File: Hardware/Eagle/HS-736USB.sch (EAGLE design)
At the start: 14 parts, among them Q1 12MHz

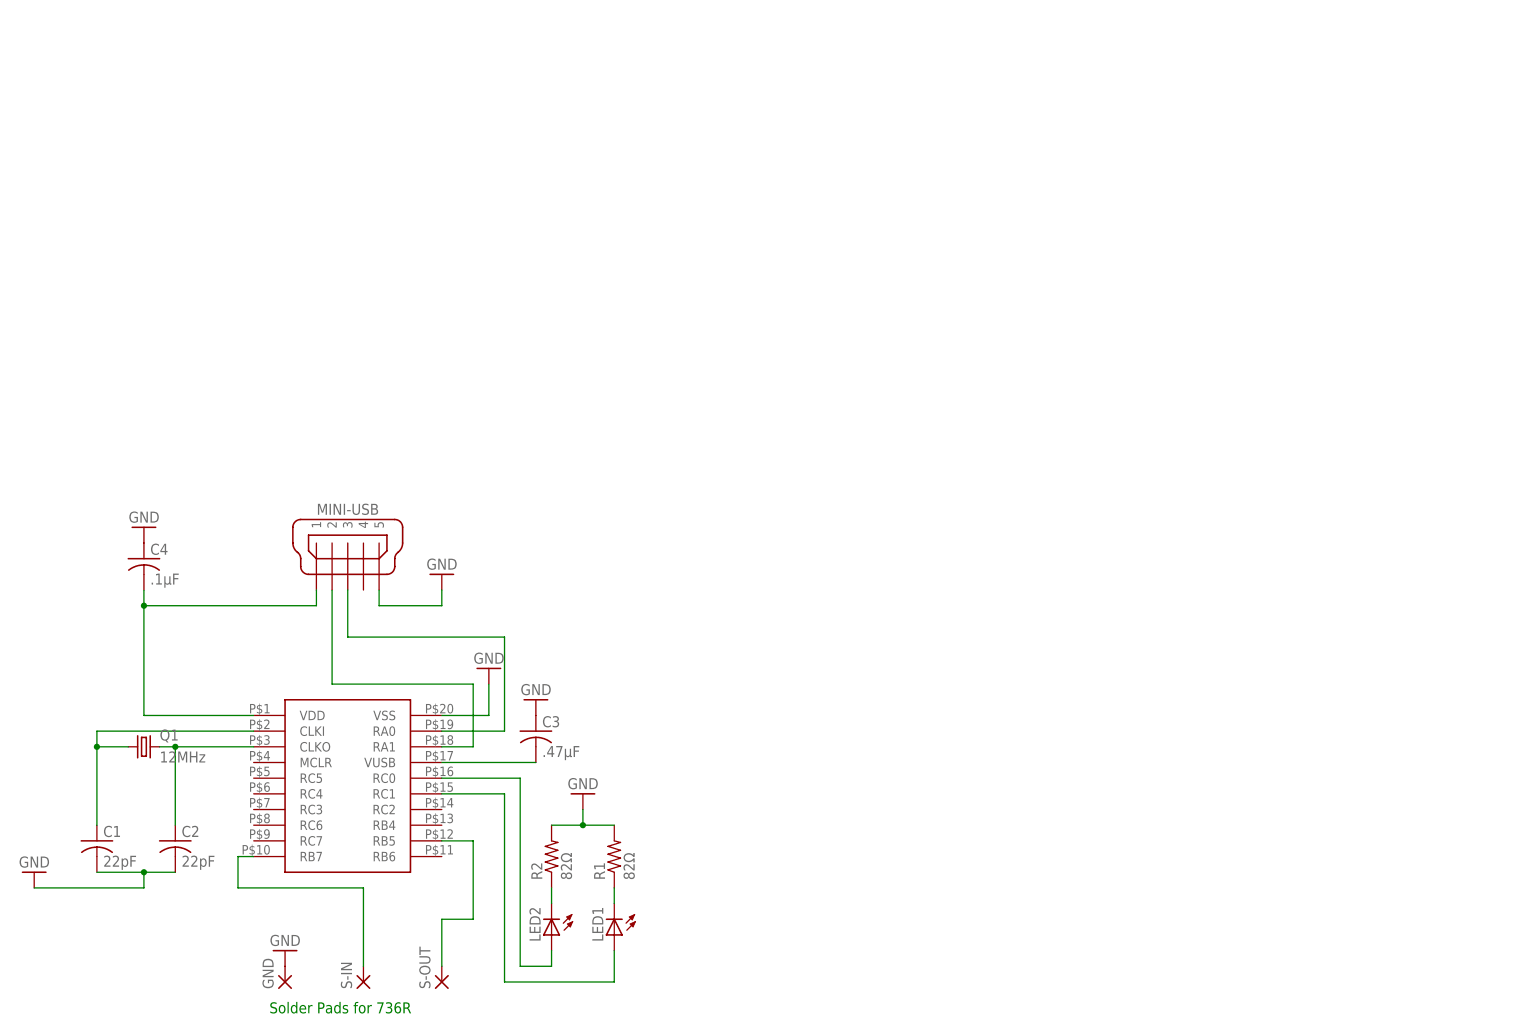
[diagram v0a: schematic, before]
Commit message: Updated schematic and board for a small board run August 2016.  Added missing Artwork for the various enclosure designs and board renderings.
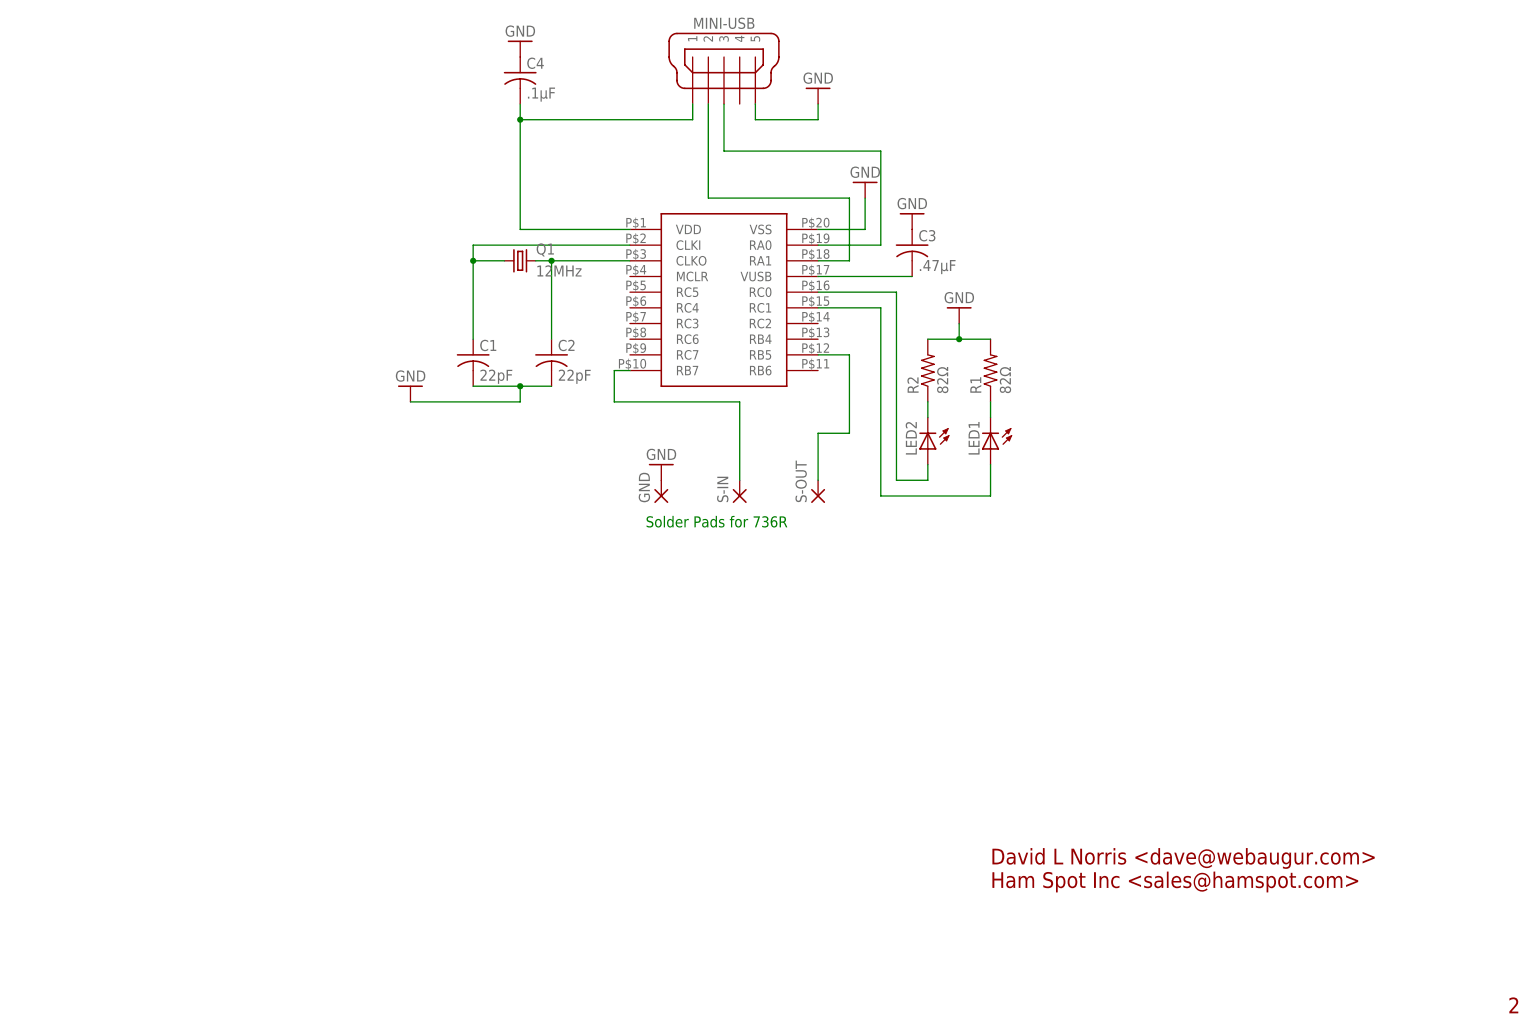
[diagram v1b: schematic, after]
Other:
- note added: "2"
- note added: "David L Norris <dave@webaugur.com> Ham Spot Inc <sales@hamspot.com>"
- moved on the sheet: C1, C2, C3, C4, GND, LED1, LED2, MINI-USB, Q1, R1, R2, S-IN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
